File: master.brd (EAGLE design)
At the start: 56.1 x 93.9 mm, 70 parts, among them IC2 MCP1703-3302, M1 DHT22-NP, M2 NRF24L01P-M, Q1 IRLML2502, Q3 25MHz, SW1 EC11E_SW, U1 XMEGA-A3TQFP, U2 DS1302SOIC, U3 25LC640A-E/SN, U4 ENC28J60SO, X1 serial, X2 SPI/1W, X3 I2C, X4 ADC, X6 PS25_3W-R, X7 PS25_3W-R, X8 PS25_3W-R, X9 PS25_3W-R

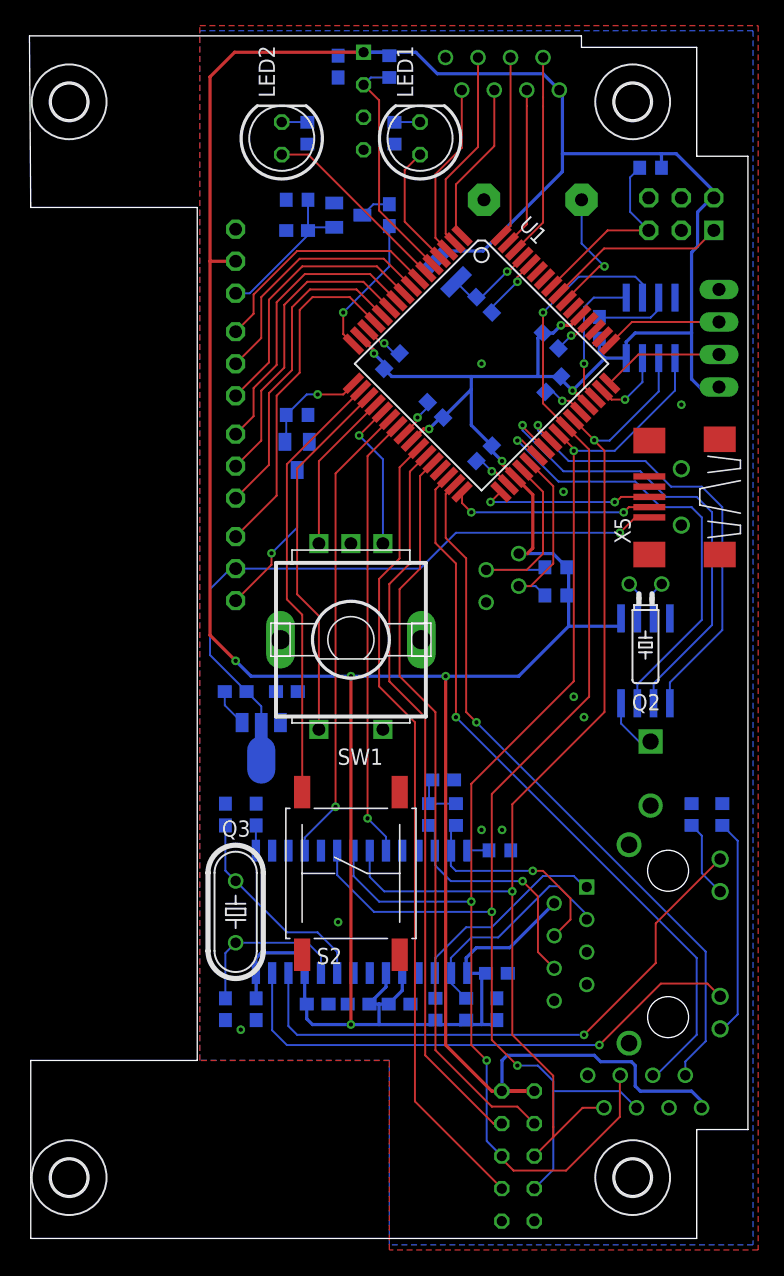
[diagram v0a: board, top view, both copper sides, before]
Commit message: added license+version information
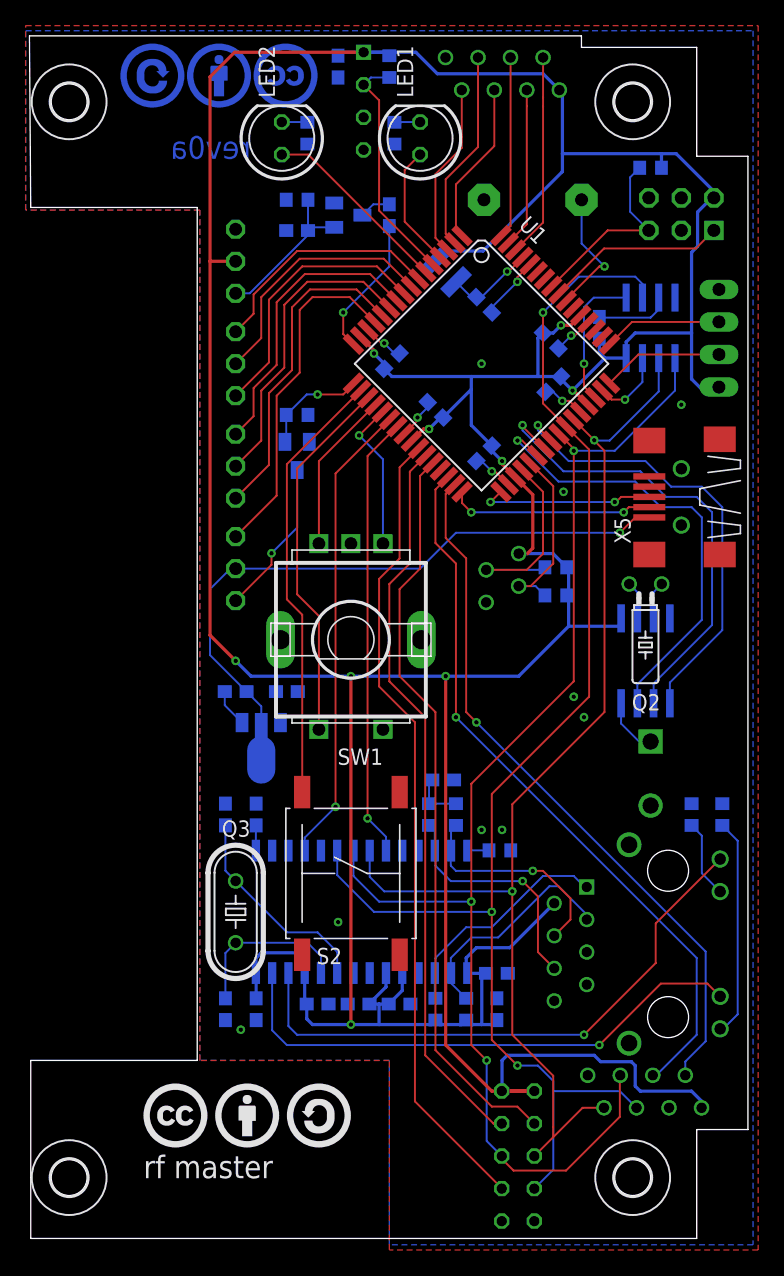
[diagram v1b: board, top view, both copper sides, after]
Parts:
- added U$1: CC-TPLACE-HALF, creative-commons:CC_TPLACE_HS
- added U$10: SA-TOP-HALF, creative-commons:SA_TOP_HS
- added U$2: BY-TPLACE-HS, creative-commons:BY_TPLACE_HS
- added U$7: SA-TPLACE-HALF, creative-commons:SA_TPLACE_HS
- added U$8: CC-TOP-HALF, creative-commons:CC_TOP_HS
- added U$9: BY-TOP-HALF, creative-commons:BY_TOP_HS
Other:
- board text added: ">BN"
- board text added: ">BR"
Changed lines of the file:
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@@
 <layer number="37" name="tTest" color="7" fill="1" visible="no" active="yes"/>
 <layer number="38" name="bTest" color="7" fill="1" visible="no" active="yes"/>
-<layer number="39" name="tKeepout" color="4" fill="11" visible="yes" active="yes"/>
-<layer number="40" name="bKeepout" color="1" fill="11" visible="yes" active="yes"/>
-<layer number="41" name="tRestrict" color="4" fill="10" visible="yes" active="yes"/>
-<layer number="42" name="bRestrict" color="1" fill="10" visible="yes" active="yes"/>
-<layer number="43" name="vRestrict" color="2" fill="10" visible="yes" active="yes"/>
-<layer number="44" name="Drills" color="7" fill="1" visible="yes" active="yes"/>
-<layer number="45" name="Holes" color="7" fill="1" visible="yes" active="yes"/>
+<layer number="39" name="tKeepout" color="4" fill="11" visible="no" active="yes"/>
+<layer number="40" name="bKeepout" color="1" fill="11" visible="no" active="yes"/>
+<layer number="41" name="tRestrict" color="4" fill="10" visible="no" active="yes"/>
+<layer number="42" name="bRestrict" color="1" fill="10" visible="no" active="yes"/>
+<layer number="43" name="vRestrict" color="2" fill="10" visible="no" active="yes"/>
+<layer number="44" name="Drills" color="7" fill="1" visible="no" active="yes"/>
+<layer number="45" name="Holes" color="7" fill="1" visible="no" active="yes"/>
 <layer number="46" name="Milling" color="3" fill="1" visible="yes" active="yes"/>
-<layer number="47" name="Measures" color="7" fill="1" visible="yes" active="yes"/>
-<layer number="48" name="Document" color="7" fill="1" visible="yes" active="yes"/>
-<layer number="49" name="Reference" color="7" fill="1" visible="yes" active="yes"/>
+<layer number="47" name="Measures" color="7" fill="1" visible="no" active="yes"/>
+<layer number="48" name="Document" color="7" fill="1" visible="no" active="yes"/>
+<layer number="49" name="Reference" color="7" fill="1" visible="no" active="yes"/>
 <layer number="50" name="dxf" color="7" fill="1" visible="no" active="no"/>
 <layer number="51" name="tDocu" color="7" fill="1" visible="no" active="yes"/>
@@
 <dimension x1="47" y1="5.25" x2="56.85" y2="6" x3="51.925" y3="35.6" textsize="1.778" layer="47" dtype="horizontal"/>
 <dimension x1="47" y1="5.25" x2="61" y2="5.2" x3="54" y3="39.2" textsize="1.778" layer="47" dtype="horizontal"/>
+<text x="8.8" y="5.2" size="1.778" layer="21" font="vector">&gt;BN</text>
+<text x="17.2" y="82.4" size="1.778" layer="16" font="vector" ratio="10" rot="MR0">&gt;BN</text>
+<text x="17.2" y="84.8" size="1.778" layer="16" font="vector" ratio="10" rot="MR0">&gt;BR</text>
+<text x="8.8" y="2.8" size="1.778" layer="21">&gt;BR</text>
 </plain>
 <attributes>
+<attribute name="BN" value="rf master"/>
+<attribute name="BR" value="rev0a"/>
 </attributes>
 <variantdefs>
@@
 </class>
 </classes>
-<designrules name="oshpark *">
+<designrules name="oshpark">
 <description language="de">&lt;a href=&quot;http://oshpark.com/guidelines&quot;&gt;http://oshpark.com/guidelines&lt;/a&gt;</description>
 <description language="en">&lt;b&gt;Laen's PCB Order Design Rules&lt;/b&gt;
@@
 <param name="dpGapFactor" value="2.5"/>
 <param name="checkGrid" value="0"/>
-<param name="checkAngle" value="0"/>
+<param name="checkAngle" value="1"/>
 <param name="checkFont" value="1"/>
 <param name="checkRestrict" value="1"/>
@@
 <attribute name="VALUE" x="49.06" y="32.965" size="1.27" layer="28" rot="MR90"/>
 </element>
+<element name="U$1" library="creative-commons" package="CC_TPLACE_HS" value="CC-TPLACE-HALF" x="8.8" y="7.6"/>
+<element name="U$2" library="creative-commons" package="BY_TPLACE_HS" value="BY-TPLACE-HS" x="14.4" y="7.6"/>
+<element name="U$7" library="creative-commons" package="SA_TPLACE_HS" value="SA-TPLACE-HALF" x="20" y="7.6"/>
+<element name="U$8" library="creative-commons" package="CC_TOP_HS" value="CC-TOP-HALF" x="22.4" y="88.8" rot="MR0"/>
+<element name="U$9" library="creative-commons" package="BY_TOP_HS" value="BY-TOP-HALF" x="17.2" y="88.8" rot="MR0"/>
+<element name="U$10" library="creative-commons" package="SA_TOP_HS" value="SA-TOP-HALF" x="12" y="88.8" rot="MR0"/>
 </elements>
 <signals>
@@
 <polygon width="0.1524" layer="16">
 <vertex x="13.2" y="14.4"/>
-<vertex x="13.2" y="94.8"/>
+<vertex x="13.2" y="80.8"/>
+<vertex x="-0.4" y="80.8"/>
+<vertex x="-0.4" y="94.8"/>
 <vertex x="56.4" y="94.8"/>
 <vertex x="56.4" y="0"/>
@@
 <vertex x="28" y="14.4"/>
 <vertex x="13.2" y="14.4"/>
+<vertex x="13.2" y="80.8"/>
+<vertex x="-0.4" y="80.8"/>
+<vertex x="-0.4" y="95.2"/>
 </polygon>
 <wire x1="15.15" y1="43.2" x2="15.15" y2="42.132" width="0.1524" layer="16"/>
@@
 </signal>
 </signals>
+<errors>
+</errors>
 </board>
 </drawing>

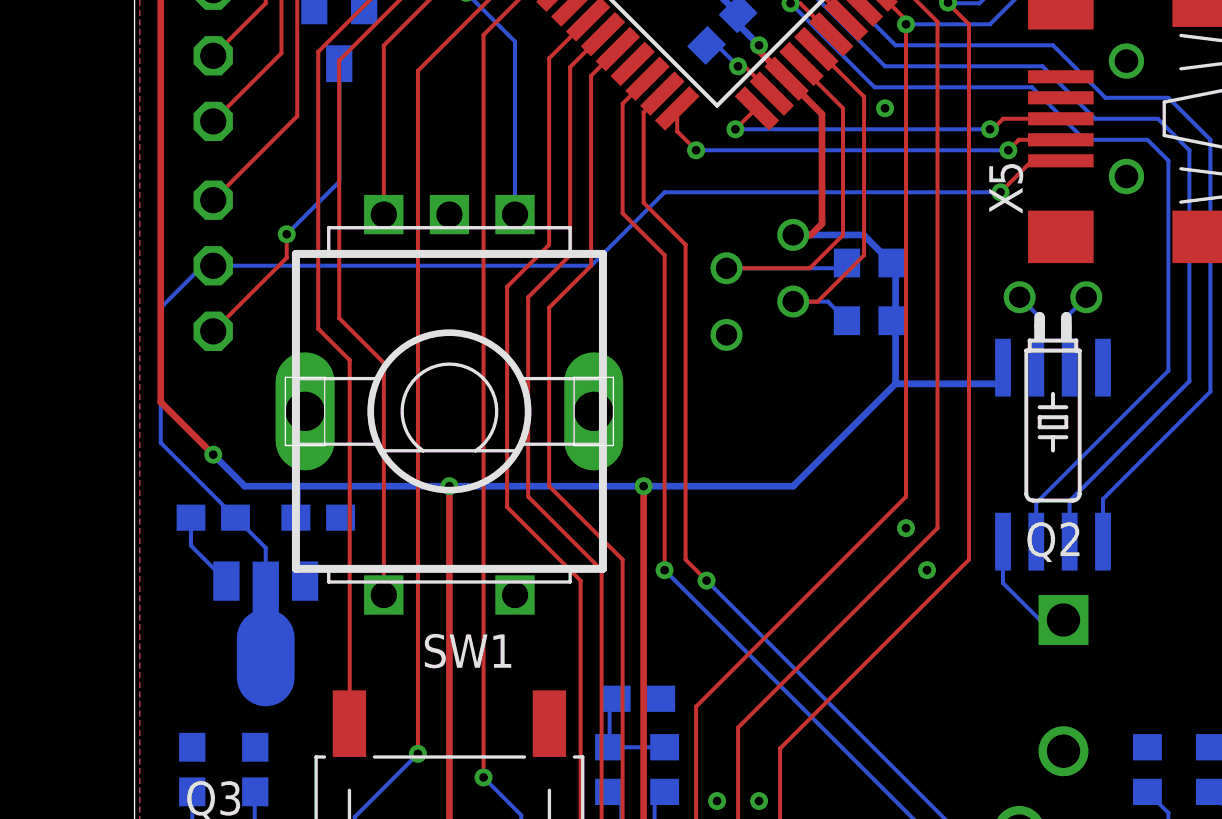
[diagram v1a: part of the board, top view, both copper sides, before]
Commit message: +5V also in netclass power with bigger width
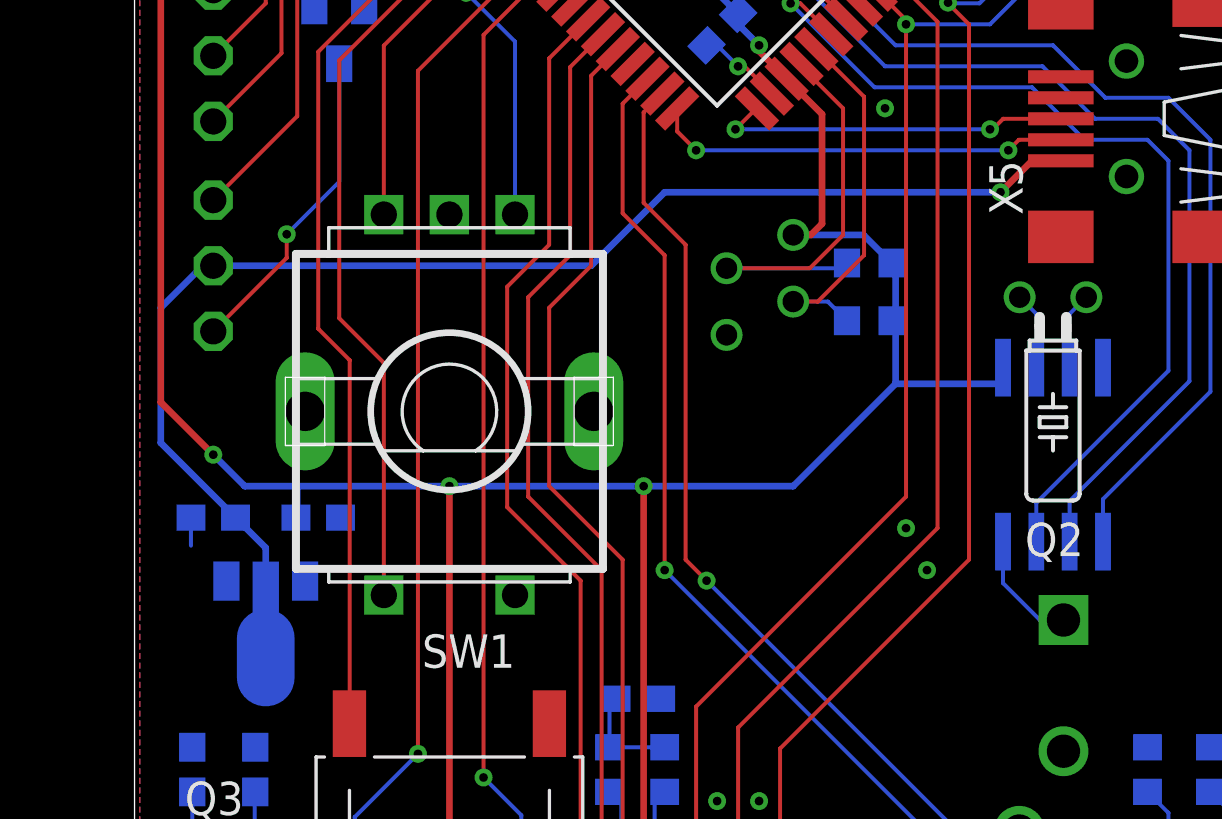
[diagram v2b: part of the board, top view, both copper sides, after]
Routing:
- net GND: track 30.1 -> 28.2 mm
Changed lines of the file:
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@@
 </polygon>
 <wire x1="15.15" y1="43.2" x2="15.15" y2="42.132" width="0.1524" layer="16"/>
-<wire x1="15.15" y1="42.132" x2="16.501" y2="40.781" width="0.1524" layer="16"/>
 <via x="35.2" y="68.8" extent="1-16" drill="0.3302" shape="octagon"/>
 <wire x1="37.2859625" y1="59.360121875" x2="36.246084375" y2="60.4" width="0.1524" layer="1"/>
@@
 <via x="41.6" y="58.8" extent="1-16" drill="0.3302" shape="octagon"/>
 </signal>
-<signal name="+5V">
+<signal name="+5V" class="1">
 <contactref element="C7" pad="1"/>
 <contactref element="X5" pad="VBUS"/>
 <contactref element="X9" pad="2"/>
-<wire x1="48.3" y1="56.8" x2="47.2" y2="56.8" width="0.1524" layer="1"/>
-<wire x1="47.2" y1="56.8" x2="46" y2="55.6" width="0.1524" layer="1"/>
+<wire x1="48.3" y1="56.8" x2="47.2" y2="56.8" width="0.254" layer="1"/>
+<wire x1="47.2" y1="56.8" x2="46" y2="55.6" width="0.254" layer="1"/>
 <via x="46" y="55.6" extent="1-16" drill="0.3302" shape="octagon"/>
-<wire x1="46" y1="55.6" x2="33.2" y2="55.6" width="0.1524" layer="16"/>
-<wire x1="33.2" y1="55.6" x2="30.4" y2="52.8" width="0.1524" layer="16"/>
-<wire x1="30.4" y1="52.8" x2="16" y2="52.8" width="0.1524" layer="16"/>
+<wire x1="46" y1="55.6" x2="33.2" y2="55.6" width="0.254" layer="16"/>
+<wire x1="33.2" y1="55.6" x2="30.4" y2="52.8" width="0.254" layer="16"/>
+<wire x1="30.4" y1="52.8" x2="16" y2="52.8" width="0.254" layer="16"/>
 <contactref element="IC2" pad="2"/>
-<wire x1="14" y1="46.05" x2="14" y2="51.2" width="0.1524" layer="16"/>
-<wire x1="14" y1="51.2" x2="15.6" y2="52.8" width="0.1524" layer="16"/>
-<wire x1="15.6" y1="52.8" x2="16" y2="52.8" width="0.1524" layer="16"/>
+<wire x1="14" y1="46.05" x2="14" y2="51.2" width="0.254" layer="16"/>
+<wire x1="14" y1="51.2" x2="15.6" y2="52.8" width="0.254" layer="16"/>
+<wire x1="15.6" y1="52.8" x2="16" y2="52.8" width="0.254" layer="16"/>
 <contactref element="IC2" pad="2@1"/>
-<wire x1="16.85" y1="43.2" x2="18" y2="42.05" width="0.1524" layer="16"/>
-<wire x1="18" y1="42.05" x2="18" y2="40.527" width="0.1524" layer="16"/>
-<wire x1="18" y1="40.527" x2="18" y2="37.86" width="0.1524" layer="16"/>
-<wire x1="14" y1="46.05" x2="16.85" y2="43.2" width="0.1524" layer="16"/>
+<wire x1="16.85" y1="43.2" x2="18" y2="42.05" width="0.254" layer="16"/>
+<wire x1="18" y1="42.05" x2="18" y2="40.527" width="0.254" layer="16"/>
+<wire x1="18" y1="40.527" x2="18" y2="37.86" width="0.254" layer="16"/>
+<wire x1="14" y1="46.05" x2="16.85" y2="43.2" width="0.254" layer="16"/>
 </signal>
 <signal name="DHTDATA">

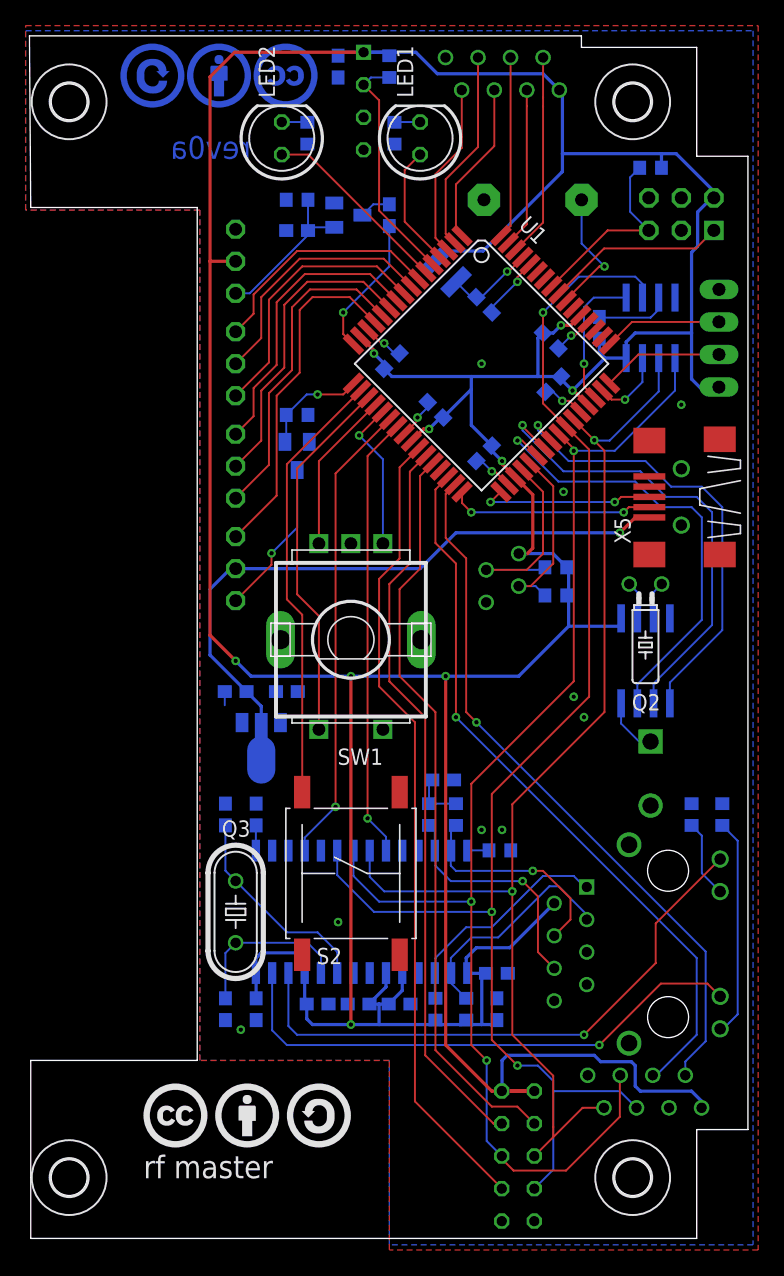
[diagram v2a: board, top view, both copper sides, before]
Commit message: improved routing
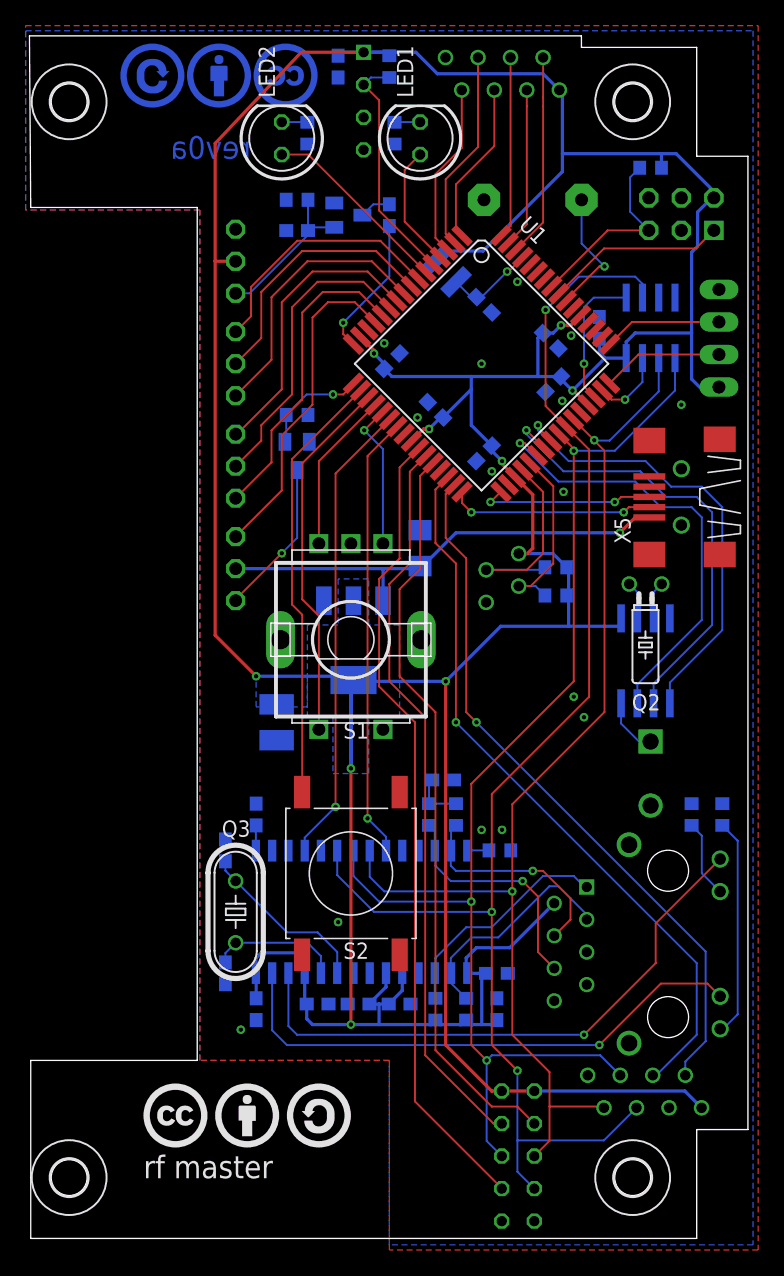
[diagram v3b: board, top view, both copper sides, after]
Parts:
- removed IC2: MCP1703-3302, karlnet-parts:SOT89
- added U5: TS1117, TS1117:SOT223
- C7: value 1u -> 10u; device rcl:C0603 -> rcl:C1206
- C8: value 1u -> 100u; device rcl:C0603 -> rcl:C1210
- moved C7 18.2 mm to (30.4, 54.4), turned to 90 degrees
- moved C22 2.80 mm to (15.2, 30.8)
- moved C23 2.80 mm to (15.2, 21.2)
- moved C8 2.53 mm to (19.2, 40.8), turned to 270 degrees
- renumbered SW1 to S1
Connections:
- net +5V: now also U5.3; no longer IC2.2, IC2.2@1
- net GND: now also U5.1; no longer IC2.1
- net VCC: now also U5.2, U5.4; no longer IC2.3
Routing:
- net GND: track 28.2 -> 0.00 mm
- net +5V: track 51.6 -> 36.8 mm
- net VCC: track 383.5 -> 373.2 mm
- net MOSI: track 100.4 -> 96.8 mm
- net N$19: track 16.5 -> 13.7 mm
- net N$18: track 13.1 -> 10.3 mm
- net LCD_D7: track 26.9 -> 25.6 mm
- net LCD_RS: track 18.7 -> 19.8 mm
- net RTC_IO: track 37.2 -> 36.1 mm
- net MISO: track 109.0 -> 110.0 mm
- net LCD_D6: track 25.2 -> 24.3 mm
- net SCK: track 91.3 -> 90.4 mm
- net LCR_RW: track 19.9 -> 20.6 mm
- net RTC_CLK: track 35.5 -> 35.0 mm
- added copper zone on layer 16, net VCC
